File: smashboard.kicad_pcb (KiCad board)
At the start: 2 copper layers, 139.1 x 76.2 mm, 78 parts, among them J1 OLED, U1 Nice_Nano_V2

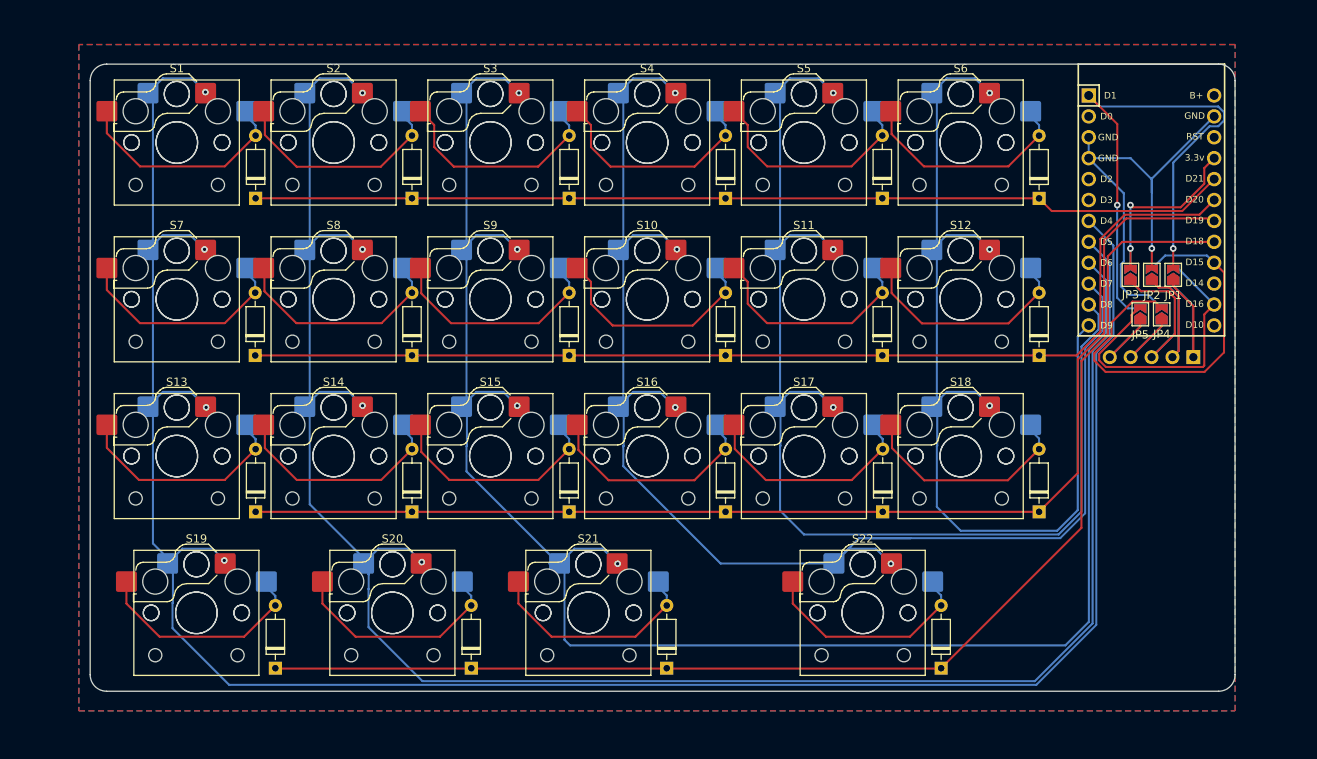
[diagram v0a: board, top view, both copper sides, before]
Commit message: PCB: Reset button, on/off button and some modification in the vias
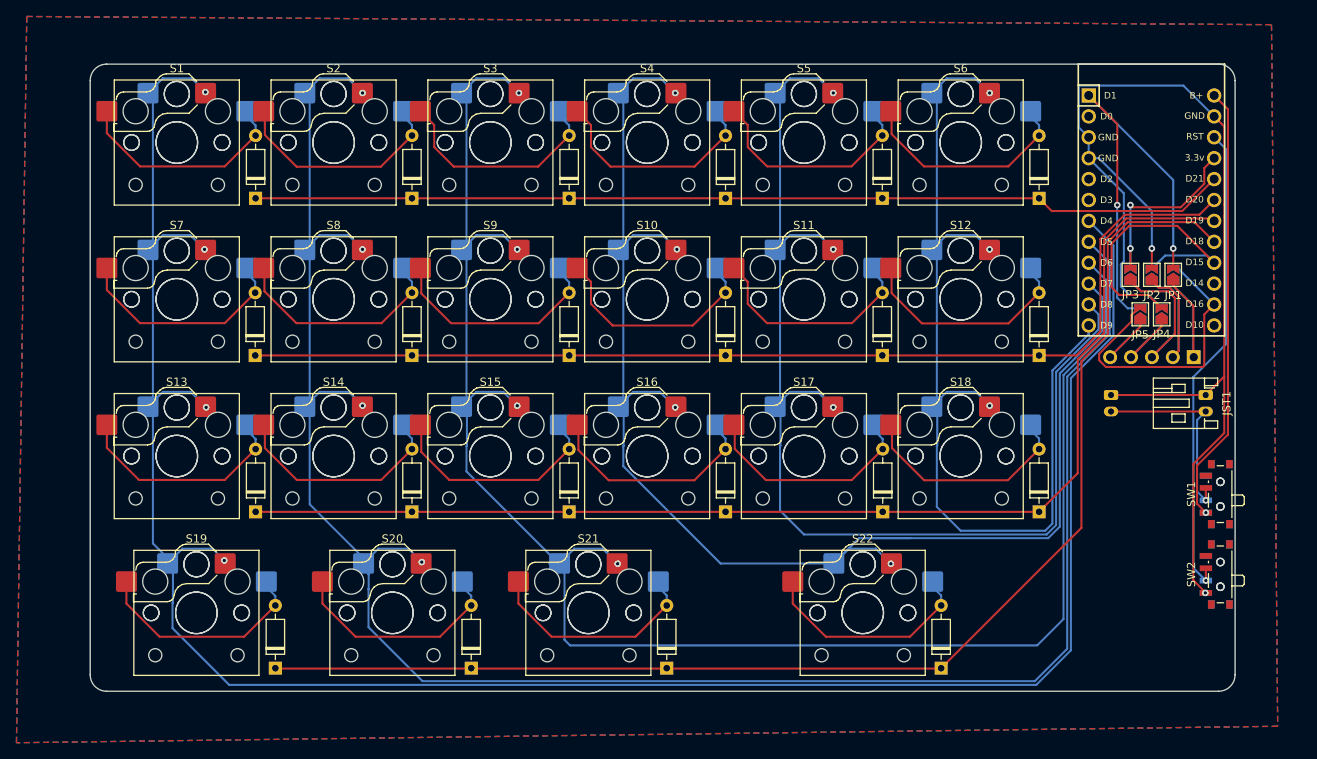
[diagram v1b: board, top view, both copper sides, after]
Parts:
- added JST1: ~, Connector_JST:JST_PH_S2B-PH-K_1x02_P2.00mm_Horizontal, F.Cu at (217.2, 94.5)
- added JST2: ~, Connector_JST:JST_PH_S2B-PH-K_1x02_P2.00mm_Horizontal, B.Cu at (205.8, 94.5)
- added SW1: SW_SPDT, Button_Switch_SMD:SW_SPDT_PCM12, F.Cu at (218.7, 106.5)
- added SW2: SW_SPDT, Button_Switch_SMD:SW_SPDT_PCM12, F.Cu at (218.7, 116.3)
- added SW3: SW_SPDT, Button_Switch_SMD:SW_SPDT_PCM12, B.Cu at (218.7, 106.5)
- added SW4: SW_SPDT, Button_Switch_SMD:SW_SPDT_PCM12, B.Cu at (218.7, 116.3)
- J1: value OLED -> OLED_128x32_Nice_View
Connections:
- net +3.3V renamed VCC
- U1 pad 22: unconnected-(U1-RST-Pad22) -> RST
- U1 pad 24: unconnected-(U1-B+-Pad24) -> B+
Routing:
- net Earth: track 58.1 -> 143.7 mm, vias 1 -> 2
- net RST: track 0.00 -> 58.2 mm, vias 0 -> 1
- net B+: track 0.00 -> 53.4 mm, vias 0 -> 1
- net Net-(JST1-VCC): track 0.00 -> 25.1 mm, vias 0 -> 1
- net CS: track 68.9 -> 54.7 mm
- net SCK: track 50.3 -> 36.3 mm
- net Row4: track 153.4 -> 156.4 mm
- net Column3: track 220.6 -> 218.6 mm
- net Column6: track 118.4 -> 117.5 mm
- net Column4: track 180.1 -> 179.3 mm
- net Column5: track 142.3 -> 141.4 mm

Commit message: Modified reset and on/off buttons footprints
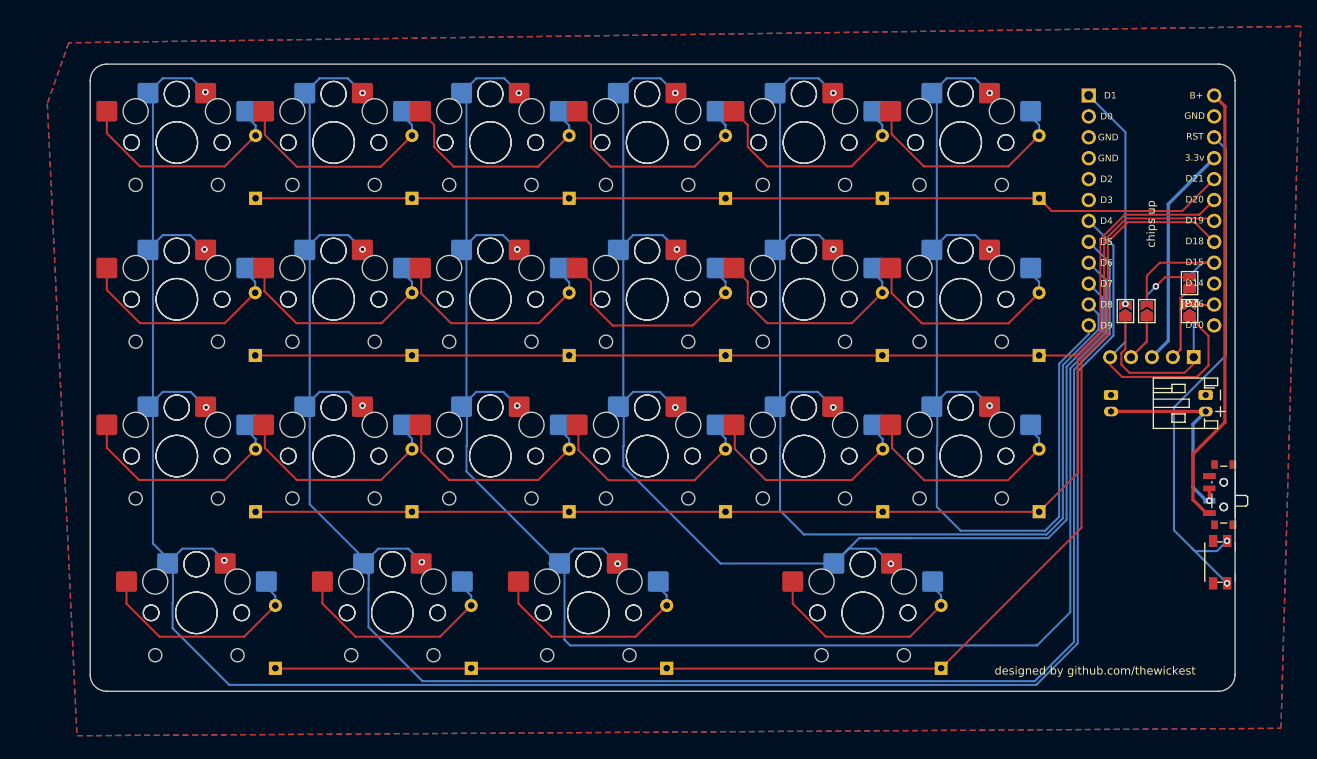
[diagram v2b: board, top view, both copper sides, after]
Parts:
- removed JP3, JP8: SolderJumper_2_Open, Jumper:SolderJumper-2_P1.3mm_Open_TrianglePad1.0x1.5mm
- S1, S10, S11, S12, S13, S14, S15, S16, S17, S18, S2, S23, S24, S25, S26, S27, S28, S29, S3, S30, S31, S32, S33, S34, S35, S36, S37, S38, S39, S4, S40, S5, S6, S7, S8, S9: footprint ScottoKeebs_Hotswap:Hotswap_Choc_V1V2_1.00u -> ScottoKeebs_Hotswap:Hotswap_Choc_V1V2
- S19, S20, S21, S41, S42, S43: footprint ScottoKeebs_Hotswap:Hotswap_Choc_V1V2_1.25u -> ScottoKeebs_Hotswap:Hotswap_Choc_V1V2
- S22, S44: footprint ScottoKeebs_Hotswap:Hotswap_Choc_V1V2_2.25u -> ScottoKeebs_Hotswap:Hotswap_Choc_V1V2
- SW2, SW4: value SW_SPDT -> SW_Push; footprint Button_Switch_SMD:SW_SPDT_PCM12 -> Button_Switch_SMD:Panasonic_EVQPUK_EVQPUB
- moved JP1 7.29 mm to (207.5, 84.3)
- moved JP5 6.00 mm to (215.3, 84.3)
- moved JP6 4.84 mm to (215.3, 84.3)
- moved JP7 4.71 mm to (215.3, 80.9)
- moved JP2 4.70 mm to (215.3, 80.9)
- moved JP10 1.85 mm to (207.5, 84.3)
- moved JP4 1.85 mm to (210.1, 84.3)
- moved JP9 1.84 mm to (210.1, 84.3)
- moved SW2 1.52 mm to (219.0, 114.8), turned to -90 degrees
- moved SW4 1.52 mm to (219.0, 114.8), turned to 90 degrees
- moved SW1 0.42 mm to (219.1, 106.6)
- moved SW3 0.42 mm to (219.1, 106.6)
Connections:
- J1 pad 3: Net-(J1-VCC) -> VCC
- JP2 pad 2: Earth -> GND
- JP9 pad 2: Earth -> GND
- JST1 pad 1: Earth -> GND
- JST2 pad 1: Earth -> GND
- SW2 pad 1: Earth -> RST
- SW2 pad 2: RST -> GND
- SW4 pad 1: unconnected-(SW4-A-Pad1) -> RST
- SW4 pad 2: RST -> GND
- U1 pad 23: Earth -> GND
- U1 pad 3: Earth -> GND
- U1 pad 4: Earth -> GND
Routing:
- net Earth: track 143.7 -> 0.00 mm, vias 2 -> 0
- net MOSI: track 36.4 -> 6.02 mm
- net Net-(J1-VCC): track 29.3 -> 0.00 mm
- net CS: track 54.7 -> 27.5 mm, vias 2 -> 1
- net SCK: track 36.3 -> 16.2 mm
- net Net-(J1-MOSI): track 12.0 -> 26.6 mm
- net GND: track 0.00 -> 7.29 mm, vias 0 -> 1
- net RST: track 58.2 -> 64.9 mm, vias 1 -> 2
- net Net-(J1-GND): track 23.4 -> 18.3 mm
- net VCC: track 24.1 -> 27.3 mm, vias 2 -> 0
- net Net-(J1-CS): track 20.6 -> 21.6 mm
- net Net-(JST1-VCC): track 25.1 -> 26.0 mm
- net Net-(J1-SCK): track 12.1 -> 11.4 mm
- net B+: track 53.4 -> 53.9 mm, vias 1 -> 0
- added copper zone on B.Cu, net GND
- added copper zone on F.Cu, net GND
- removed copper zone on B.Cu, net (none)
- removed copper zone on F.Cu, net (none)
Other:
- board text added: "chips down"
- board text added: "chips up"
- board text added: "designed by github.com/thewickest"

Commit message: Some errors after changing the switch footprint
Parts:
- moved SW1 0.20 mm to (218.9, 106.6)
- moved SW3 0.20 mm to (218.9, 106.6)
- moved U1 0.06 mm to (210.6, 72.1)
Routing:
- net GND: vias 1 -> 2
- net B+: vias 0 -> 1
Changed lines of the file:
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@@
     (property "ki_keywords" "solder jumper SPST")
     (attr exclude_from_pos_files)
-    (fp_text reference "JP2" (at -2.475 0) (layer "F.SilkS")
+    (fp_text reference "JP2" (at -2.475 0) (layer "F.SilkS") hide
         (effects (font (size 1 1) (thickness 0.15)))
     )
@@
   )
   (footprint "Button_Switch_SMD:SW_SPDT_PCM12" (layer "F.Cu")
-    (at 219.125 106.6 90)
+    (at 218.925 106.6 90)
     (descr "Ultraminiature Surface Mount Slide Switch, right-angle, https://www.ckswitches.com/media/1424/pcm.pdf")
     (property "Sheetfile" "smashboard.kicad_sch")
@@
   )
   (footprint "ScottoKeebs_MCU:Nice_Nano_V2" (layer "F.Cu")
-    (at 210.66125 72.0725)
+    (at 210.6 72.0725)
     (property "Sheetfile" "smashboard.kicad_sch")
     (property "Sheetname" "")
@@
     (property "ki_keywords" "solder jumper SPST")
     (attr exclude_from_pos_files)
-    (fp_text reference "JP6" (at -2.4 0) (layer "B.SilkS") hide
+    (fp_text reference "JP6" (at 1.6 -6.6) (layer "B.SilkS") hide
         (effects (font (size 1 1) (thickness 0.15)) (justify mirror))
     )
-    (fp_text value "SolderJumper_2_Open" (at 0 -1.9 90) (layer "B.Fab") hide
+    (fp_text value "SolderJumper_2_Open" (at 0 -1.9 -90) (layer "B.Fab") hide
         (effects (font (size 1 1) (thickness 0.15)) (justify mirror))
     )
@@
     (property "ki_keywords" "solder jumper SPST")
     (attr exclude_from_pos_files)
-    (fp_text reference "JP7" (at -2.4 0) (layer "B.SilkS")
+    (fp_text reference "JP7" (at -2.4 0) (layer "B.SilkS") hide
         (effects (font (size 1 1) (thickness 0.15)) (justify mirror))
     )
-    (fp_text value "SolderJumper_2_Open" (at 0 -1.9 90) (layer "B.Fab") hide
+    (fp_text value "SolderJumper_2_Open" (at 0 -1.9 -90) (layer "B.Fab") hide
         (effects (font (size 1 1) (thickness 0.15)) (justify mirror))
     )
@@
   )
   (footprint "Button_Switch_SMD:SW_SPDT_PCM12" (layer "B.Cu")
-    (at 219.125 106.6 -90)
+    (at 218.925 106.6 -90)
     (descr "Ultraminiature Surface Mount Slide Switch, right-angle, https://www.ckswitches.com/media/1424/pcm.pdf")
     (property "Sheetfile" "smashboard.kicad_sch")
@@
   (segment (start 217.33625 108.85) (end 215.70875 107.2225) (width 0.4) (layer "F.Cu") (net 48))
   (segment (start 219.59 59.41125) (end 218.28125 58.1025) (width 0.4) (layer "F.Cu") (net 48))
+  (via (at 217.495 108.85) (size 0.8) (drill 0.4) (layers "F.Cu" "B.Cu") (net 48))
   (segment (start 217.75 104.35) (end 217.8 104.4) (width 0.25) (layer "B.Cu") (net 50))
   (segment (start 217.695 104.35) (end 217.75 104.35) (width 0.25) (layer "B.Cu") (net 50))
   (segment (start 212.325 80.175) (end 215.3 80.175) (width 0.25) (layer "F.Cu") (net 51))
   (segment (start 211.2 81.3) (end 212.325 80.175) (width 0.25) (layer "F.Cu") (net 51))
+  (via (at 218.15 112.225) (size 0.8) (drill 0.4) (layers "F.Cu" "B.Cu") (net 51))
   (via (at 211.2 81.3) (size 0.8) (drill 0.4) (layers "F.Cu" "B.Cu") (net 51))
   (segment (start 210.10875 82.39125) (end 210.10875 83.5675) (width 0.25) (layer "B.Cu") (net 51))
